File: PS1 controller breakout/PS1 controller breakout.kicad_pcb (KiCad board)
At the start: 2 copper layers, 30 x 40 mm, 3 parts, among them J1 PSX Controller 1P, J2 JST-PH, J3 Conn_01x09_Pin

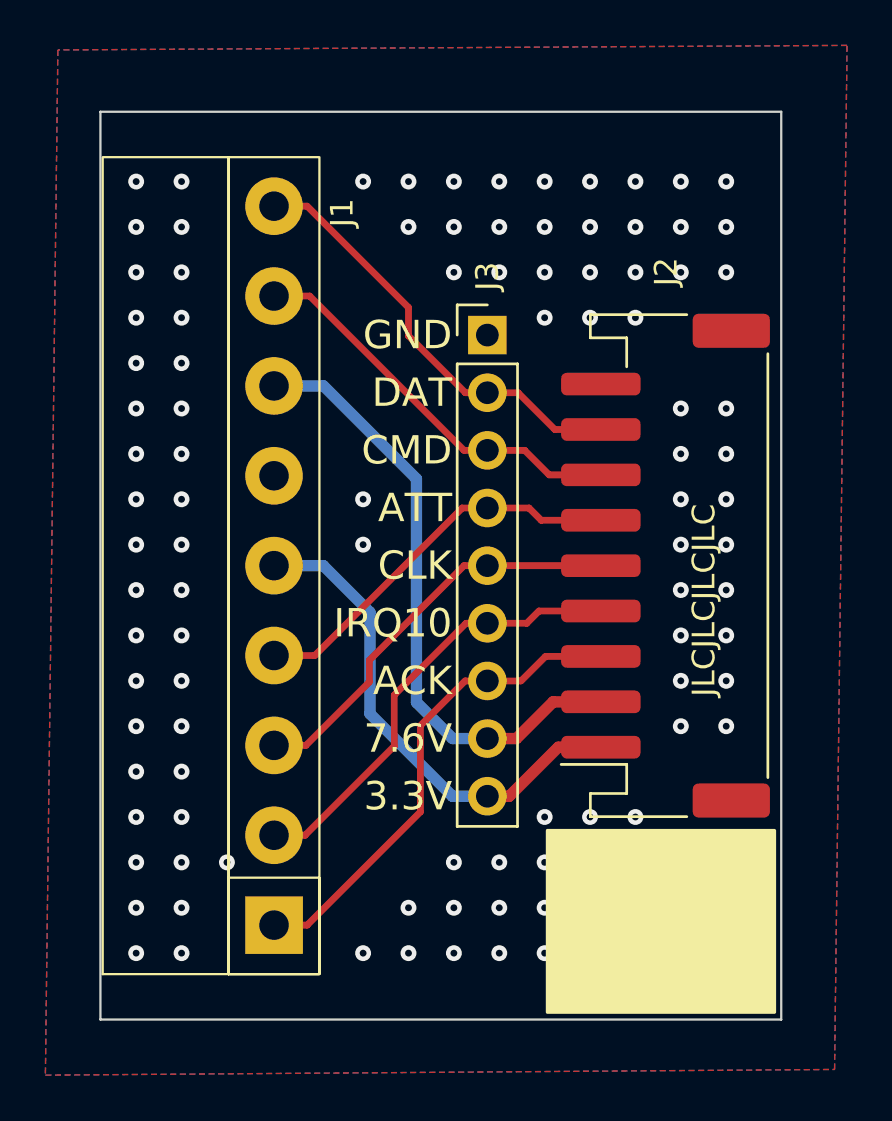
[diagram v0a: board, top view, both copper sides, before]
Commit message: updated PCBs for JLCs new erial numbering system
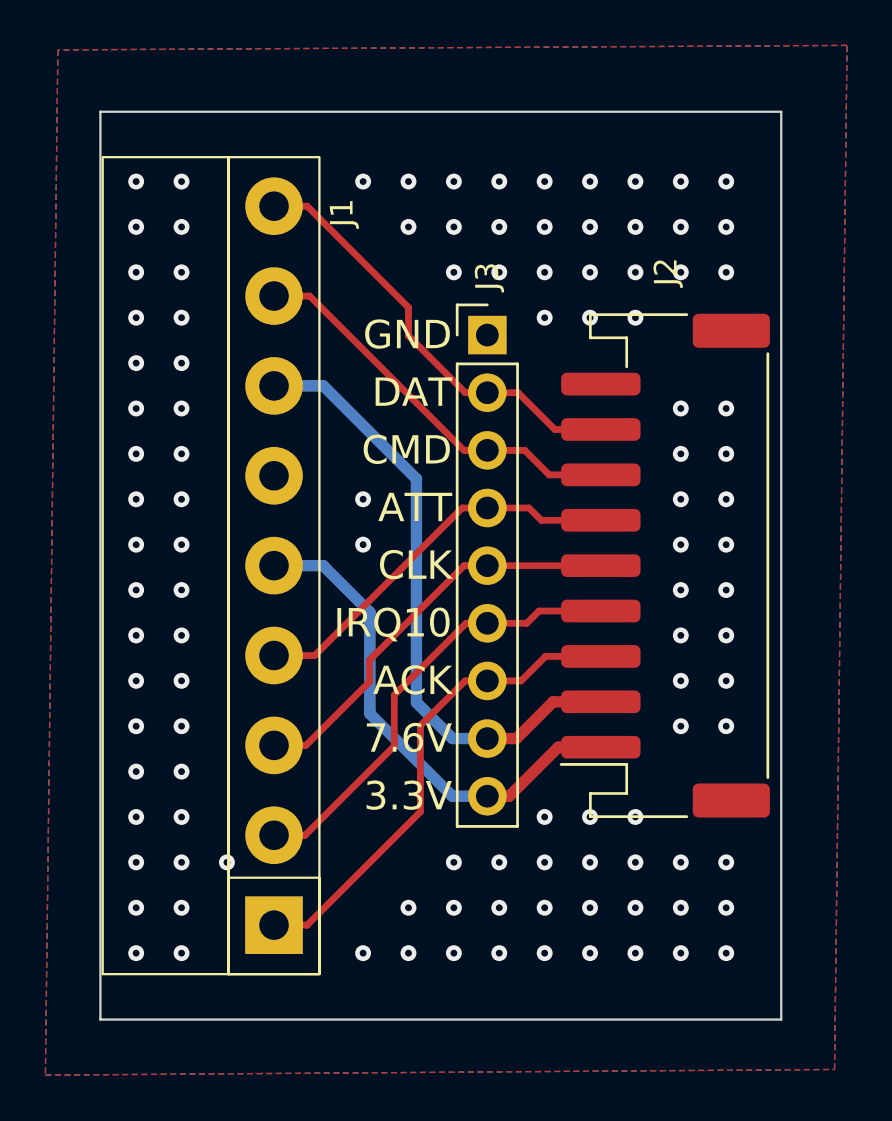
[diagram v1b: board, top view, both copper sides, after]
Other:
- board text added: "PSX JST EDU v1"
- board text removed: "JLCJLCJLCJLC"
